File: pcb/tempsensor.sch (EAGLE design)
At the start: 28 parts, among them Q1 DS18X20TO92, Q2 DS18X20SO-8, U1 ESP8266, U2 MCP73831T-2DCI/OT, X1 MINI-USB-32005-201

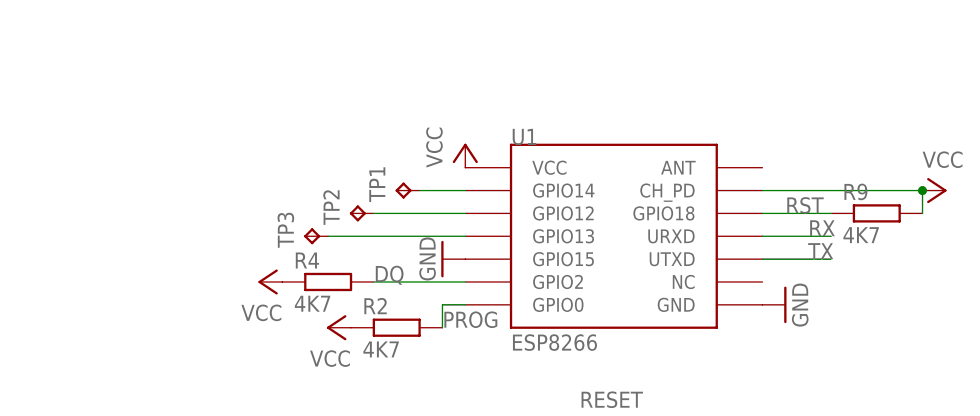
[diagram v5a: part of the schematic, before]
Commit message: PCB: rename testpoints, add points for VCC and GND, add RP-SMA connector for external antenna
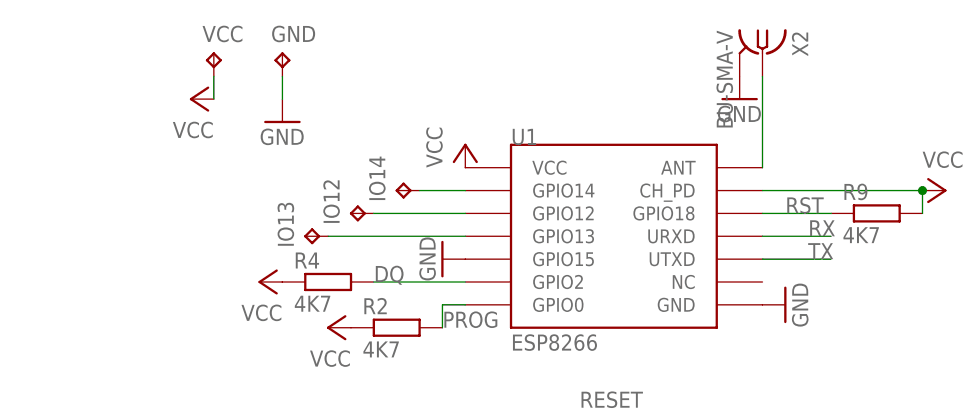
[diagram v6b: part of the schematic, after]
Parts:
- added GND, VCC: TPPAD1-13, testpad:TPPAD1-13
- added X2: BU-SMA-V, con-coax:BU-SMA-V
- renumbered TP1 to IO14, TP2 to IO12, TP3 to IO13
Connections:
- new net N$7: U1.ANT, X2.1
- net GND: now also GND.TP, X2.2
- net VCC: now also VCC.TP
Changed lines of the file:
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@@
 <?xml version="1.0" encoding="utf-8"?>
 <!DOCTYPE eagle SYSTEM "eagle.dtd">
-<eagle version="7.2.0">
+<eagle version="7.4.0">
 <drawing>
 <settings>
@@
 <part name="P+1" library="supply1" deviceset="VCC" device=""/>
 <part name="FRAME1" library="frames" deviceset="A4L-LOC" device=""/>
-<part name="TP1" library="testpad" deviceset="TP" device="PAD1-13"/>
-<part name="TP2" library="testpad" deviceset="TP" device="PAD1-13"/>
-<part name="TP3" library="testpad" deviceset="TP" device="PAD1-13"/>
+<part name="IO14" library="testpad" deviceset="TP" device="PAD1-13"/>
+<part name="IO12" library="testpad" deviceset="TP" device="PAD1-13"/>
+<part name="IO13" library="testpad" deviceset="TP" device="PAD1-13"/>
 <part name="T1" library="zetex" deviceset="NMOSSOT23" device=""/>
 <part name="R1" library="resistor" deviceset="R-EU_" device="M0805" value="10k"/>
@@
 <part name="R9" library="resistor" deviceset="R-EU_" device="M0805" value="4K7"/>
 <part name="C4" library="resistor" deviceset="C-EU" device="C1206" value="100u"/>
+<part name="VCC" library="testpad" deviceset="TP" device="PAD1-13"/>
+<part name="GND" library="testpad" deviceset="TP" device="PAD1-13"/>
+<part name="P+14" library="supply1" deviceset="VCC" device=""/>
+<part name="GND15" library="supply1" deviceset="GND" device=""/>
+<part name="X2" library="con-coax" deviceset="BU-SMA-V" device=""/>
+<part name="GND16" library="supply1" deviceset="GND" device=""/>
 </parts>
 <sheets>
@@
 <instance part="P+1" gate="VCC" x="149.86" y="127" rot="R270"/>
 <instance part="FRAME1" gate="G$1" x="-83.82" y="-27.94"/>
-<instance part="TP1" gate="G$1" x="88.9" y="127" rot="R90"/>
-<instance part="TP2" gate="G$1" x="83.82" y="124.46" rot="R90"/>
-<instance part="TP3" gate="G$1" x="78.74" y="121.92" rot="R90"/>
+<instance part="IO14" gate="G$1" x="88.9" y="127" rot="R90"/>
+<instance part="IO12" gate="G$1" x="83.82" y="124.46" rot="R90"/>
+<instance part="IO13" gate="G$1" x="78.74" y="121.92" rot="R90"/>
 <instance part="T1" gate="A" x="17.78" y="33.02" rot="R270"/>
 <instance part="R1" gate="G$1" x="10.16" y="38.1" rot="R90"/>
@@
 <instance part="R9" gate="G$1" x="142.24" y="124.46"/>
 <instance part="C4" gate="G$1" x="83.82" y="78.74" rot="R270"/>
+<instance part="VCC" gate="G$1" x="68.58" y="142.24"/>
+<instance part="GND" gate="G$1" x="76.2" y="142.24"/>
+<instance part="P+14" gate="VCC" x="66.04" y="137.16" rot="R90"/>
+<instance part="GND15" gate="1" x="76.2" y="134.62"/>
+<instance part="X2" gate="G$1" x="129.54" y="142.24" rot="R270"/>
+<instance part="GND16" gate="1" x="127" y="137.16"/>
 </instances>
 <busses>
@@
 <wire x1="10.16" y1="109.22" x2="10.16" y2="104.14" width="0.1524" layer="91"/>
 </segment>
+<segment>
+<pinref part="VCC" gate="G$1" pin="TP"/>
+<pinref part="P+14" gate="VCC" pin="VCC"/>
+<wire x1="68.58" y1="137.16" x2="68.58" y2="139.7" width="0.1524" layer="91"/>
+</segment>
 </net>
 <net name="GND" class="0">
@@
 <pinref part="GND14" gate="1" pin="GND"/>
 </segment>
+<segment>
+<pinref part="GND" gate="G$1" pin="TP"/>
+<pinref part="GND15" gate="1" pin="GND"/>
+<wire x1="76.2" y1="137.16" x2="76.2" y2="139.7" width="0.1524" layer="91"/>
+</segment>
+<segment>
+<pinref part="X2" gate="G$1" pin="2"/>
+<pinref part="GND16" gate="1" pin="GND"/>
+</segment>
 </net>
 <net name="RX" class="0">
@@
 <segment>
 <pinref part="U1" gate="G$1" pin="GPIO13"/>
-<pinref part="TP3" gate="G$1" pin="TP"/>
+<pinref part="IO13" gate="G$1" pin="TP"/>
 <wire x1="96.52" y1="121.92" x2="81.28" y2="121.92" width="0.1524" layer="91"/>
 </segment>
@@
 <net name="N$3" class="0">
 <segment>
-<pinref part="TP2" gate="G$1" pin="TP"/>
+<pinref part="IO12" gate="G$1" pin="TP"/>
 <pinref part="U1" gate="G$1" pin="GPIO12"/>
 <wire x1="86.36" y1="124.46" x2="96.52" y2="124.46" width="0.1524" layer="91"/>
@@
 <segment>
 <pinref part="U1" gate="G$1" pin="GPIO14"/>
-<pinref part="TP1" gate="G$1" pin="TP"/>
+<pinref part="IO14" gate="G$1" pin="TP"/>
 <wire x1="96.52" y1="127" x2="91.44" y2="127" width="0.1524" layer="91"/>
 </segment>
@@
 </segment>
 </net>
+<net name="N$7" class="0">
+<segment>
+<pinref part="X2" gate="G$1" pin="1"/>
+<pinref part="U1" gate="G$1" pin="ANT"/>
+<wire x1="129.54" y1="139.7" x2="129.54" y2="129.54" width="0.1524" layer="91"/>
+</segment>
+</net>
